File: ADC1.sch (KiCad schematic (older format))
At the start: 28 parts, among them U35 LTC2320CUKG-12#PBF

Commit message: PVT
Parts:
- C138: renamed from C143; PartName C1005X5R1V105K050BE -> TMK105BJ105MV-F
- renumbered C134 to C129, C135 to C130, C136 to C131, C137 to C132, C138 to C133, C139 to C134, C140 to C135, C141 to C136, C142 to C137, C144 to C139, C145 to C140, C146 to C141, C147 to C142, C148 to C143, C149 to C144, C150 to C145, C151 to C146, C152 to C147, C153 to C148, RA11 to RA12, RA12 to RA13, RA13 to RA14, RA14 to RA15, RA15 to RA16, RA16 to RA17, RA17 to RA18, U35 to U33

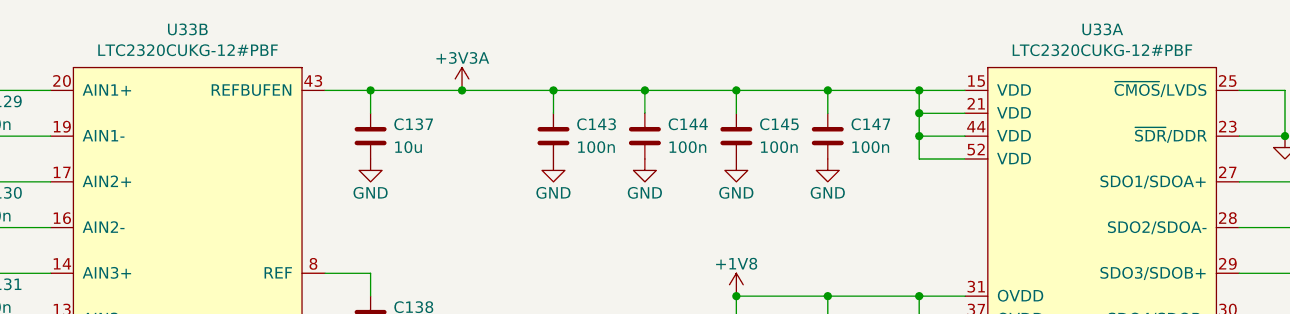
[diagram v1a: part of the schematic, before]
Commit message: SBUにTVSダイオードを追加
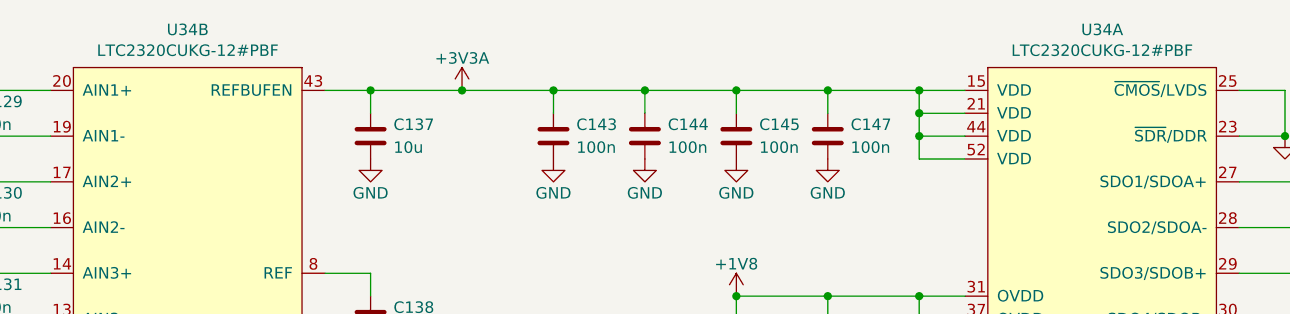
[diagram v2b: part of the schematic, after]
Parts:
- renumbered U33 to U34
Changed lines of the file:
@@
 $EndDescr
 $Comp
-L analog-lt:LTC2320 U33
+L analog-lt:LTC2320 U34
 U 1 1 5E3CE584
 P 7500 4000
-F 0 "U33" H 7500 5665 50  0000 C CNN
+F 0 "U34" H 7500 5665 50  0000 C CNN
 F 1 "LTC2320CUKG-12#PBF" H 7500 5574 50  0000 C CNN
 F 2 "IC-QFN:QFN52_7.0x8.0_P0.5_EP5.41x6.45" H 7500 4000 50  0001 C CNN
@@
 $EndComp
 $Comp
-L analog-lt:LTC2320 U33
+L analog-lt:LTC2320 U34
 U 2 1 5E3CF7D0
 P 3500 4100
-F 0 "U33" H 3500 5865 50  0000 C CNN
+F 0 "U34" H 3500 5865 50  0000 C CNN
 F 1 "LTC2320CUKG-12#PBF" H 3500 5774 50  0000 C CNN
 F 2 "IC-QFN:QFN52_7.0x8.0_P0.5_EP5.41x6.45" H 3500 4100 50  0001 C CNN
